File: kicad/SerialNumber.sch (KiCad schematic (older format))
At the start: 0 parts

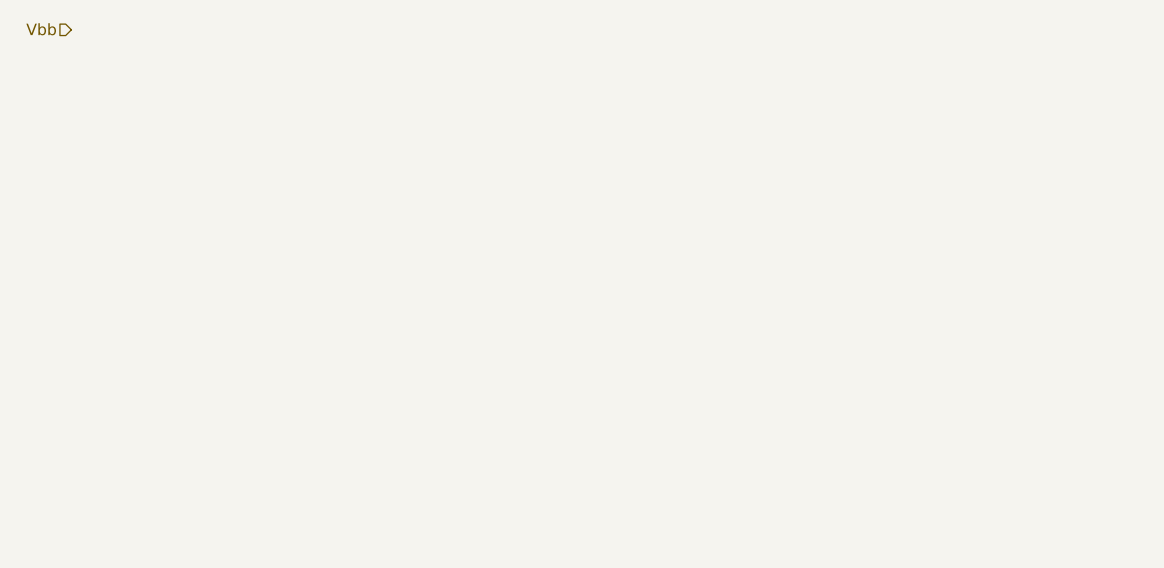
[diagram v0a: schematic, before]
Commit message: First draft of some of the sub-sheets
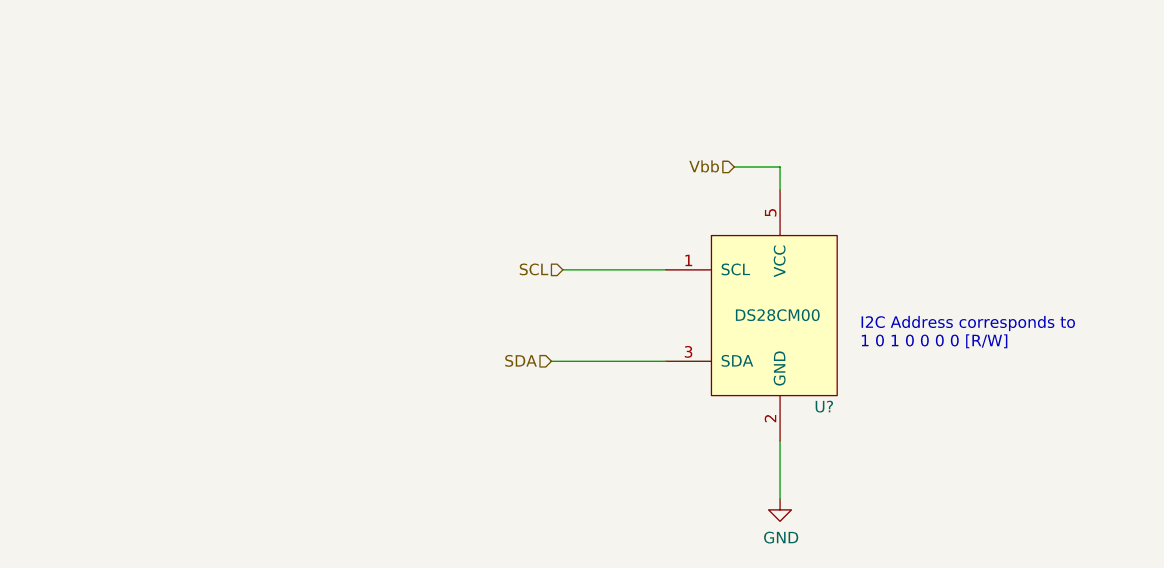
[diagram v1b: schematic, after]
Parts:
- added U?: DS28CM00, symbol FieldDevice_R2:DS28CM00
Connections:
- net Vbb: now also U?.5 (VCC)
- new net GND: U?.2 (GND)
- new net SCL: U?.1 (SCL)
- new net SDA: U?.3 (SDA)
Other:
- note added: "I2C Address corresponds to \n1 0 1 0 0 0 0 [R/W]"
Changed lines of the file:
@@
 EESchema Schematic File Version 4
 LIBS:FieldDevice_R2-cache
+LIBS:FieldDevice_Power_5V-cache
 EELAYER 26 0
 EELAYER END
 $Descr A4 11693 8268
 encoding utf-8
-Sheet 4 8
+Sheet 3 8
 Title ""
 Date ""
@@
 Comment4 ""
 $EndDescr
-Text HLabel 2150 2000 0    50   Input ~ 0
+Text HLabel 5050 2600 0    50   Input ~ 0
 Vbb
+$Comp
+L FieldDevice_R2:DS28CM00 U?
+U 1 1 5C6B2A67
+P 5250 3250
+F 0 "U?" H 5400 2850 50  0000 L CNN
+F 1 "DS28CM00" H 5050 3250 50  0000 L CNN
+F 2 "" H 5250 3250 50  0001 C CNN
+F 3 "" H 5250 3250 50  0001 C CNN
+	1    5250 3250
+	1    0    0    -1
+$EndComp
+$Comp
+L FieldDevice_Power_5V-rescue:GND #PWR?
+U 1 1 5C6B2B0B
+P 5250 4050
+F 0 "#PWR?" H 5250 3800 50  0001 C CNN
+F 1 "GND" H 5255 3877 50  0000 C CNN
+F 2 "" H 5250 4050 50  0001 C CNN
+F 3 "" H 5250 4050 50  0001 C CNN
+	1    5250 4050
+	1    0    0    -1
+$EndComp
+Wire Wire Line
+	5250 3800 5250 4050
+Wire Wire Line
+	5050 2600 5250 2600
+Wire Wire Line
+	5250 2600 5250 2700
+Text HLabel 4250 3450 0    50   Input ~ 0
+SDA
+Wire Wire Line
+	4250 3450 4750 3450
+Wire Wire Line
+	4750 3050 4300 3050
+Text HLabel 4300 3050 0    50   Input ~ 0
+SCL
+Text Notes 5600 3400 0    50   ~ 0
+I2C Address corresponds to \n1 0 1 0 0 0 0 [R/W]
 $EndSCHEMATC

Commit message: Revision 3
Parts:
- U?: Link (none) -> https://www.digikey.de/product-detail/de/maxim-integrated/D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; MPN (none) -> DS28CM00R-A00+T
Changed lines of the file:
@@
 F 1 "DS28CM00" H 5050 3250 50  0000 L CNN
 F 2 "" H 5250 3250 50  0001 C CNN
-F 3 "" H 5250 3250 50  0001 C CNN
+F 3 "https://datasheets.maximintegrated.com/en/ds/DS28CM00.pdf" H 5250 3250 50  0001 C CNN
+F 4 "DS28CM00R-A00+T" H 5250 3250 50  0001 C CNN "MPN"
+F 5 "https://www.digikey.de/product-detail/de/maxim-integrated/DS28CM00R-A00-T/DS28CM00R-A00-TCT-ND/2699348" H 5250 3250 50  0001 C CNN "Link"
 	1    5250 3250
 	1    0    0    -1
